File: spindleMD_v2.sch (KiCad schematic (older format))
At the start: 0 parts

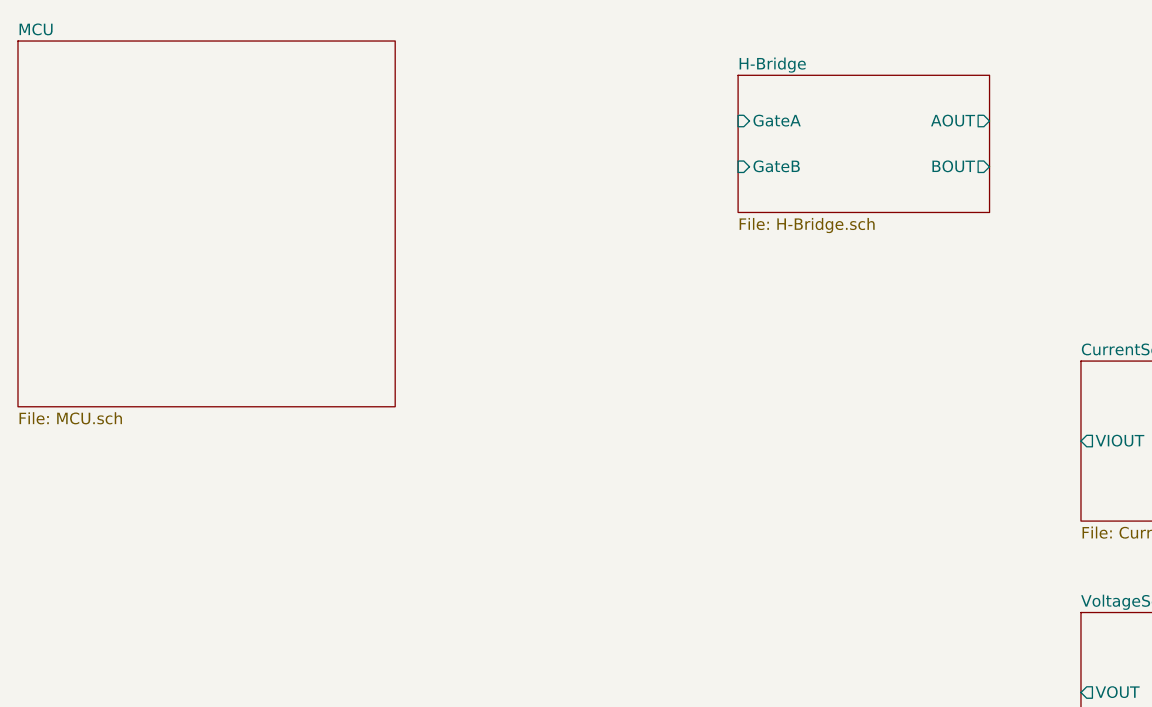
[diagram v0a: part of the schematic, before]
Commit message: デッドタイム挿入回路を削除、マイコンブロック作成
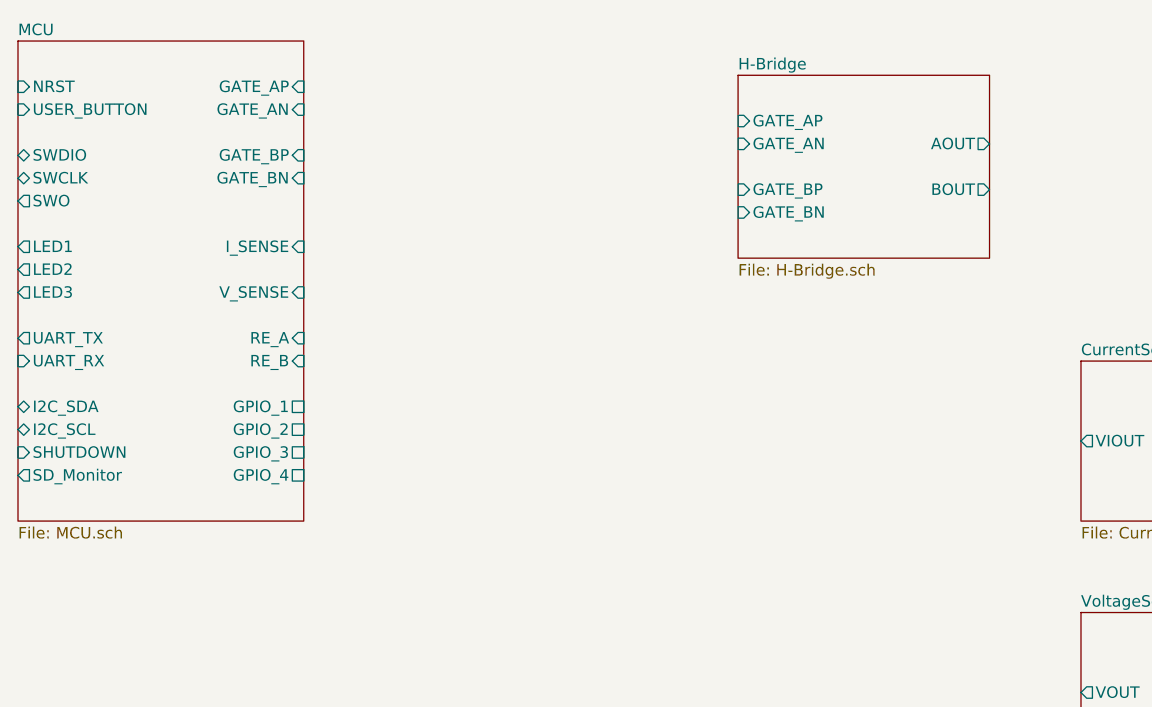
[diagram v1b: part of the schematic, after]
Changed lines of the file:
@@
 $EndDescr
 $Sheet
-S 3700 2550 1650 1600
+S 3700 2550 1250 2100
 U 5C77D603
 F0 "MCU" 50
 F1 "MCU.sch" 50
+F2 "NRST" I L 3700 2750 50
+F3 "SWDIO" B L 3700 3050 50
+F4 "SWCLK" B L 3700 3150 50
+F5 "SWO" O L 3700 3250 50
+F6 "I_SENSE" I R 4950 3450 50
+F7 "V_SENSE" I R 4950 3650 50
+F8 "GATE_AP" I R 4950 2750 50
+F9 "GATE_AN" I R 4950 2850 50
+F10 "GATE_BP" I R 4950 3050 50
+F11 "GATE_BN" I R 4950 3150 50
+F12 "UART_TX" O L 3700 3850 50
+F13 "UART_RX" I L 3700 3950 50
+F14 "I2C_SDA" B L 3700 4150 50
+F15 "I2C_SCL" B L 3700 4250 50
+F16 "RE_A" I R 4950 3850 50
+F17 "RE_B" I R 4950 3950 50
+F18 "LED1" O L 3700 3450 50
+F19 "LED2" O L 3700 3550 50
+F20 "LED3" O L 3700 3650 50
+F21 "USER_BUTTON" I L 3700 2850 50
+F22 "SD_Monitor" O L 3700 4450 50
+F23 "SHUTDOWN" I L 3700 4350 50
+F24 "GPIO_1" U R 4950 4150 50
+F25 "GPIO_2" U R 4950 4250 50
+F26 "GPIO_3" U R 4950 4350 50
+F27 "GPIO_4" U R 4950 4450 50
 $EndSheet
 $Sheet
-S 6850 2700 1100 600
+S 6850 2700 1100 800
 U 5C77D64E
 F0 "H-Bridge" 50
 F1 "H-Bridge.sch" 50
-F2 "AOUT" O R 7950 2900 50
-F3 "BOUT" O R 7950 3100 50
-F4 "GateA" I L 6850 2900 50
-F5 "GateB" I L 6850 3100 50
+F2 "AOUT" O R 7950 3000 50
+F3 "BOUT" O R 7950 3200 50
+F4 "GATE_AP" I L 6850 2900 50
+F5 "GATE_AN" I L 6850 3000 50
+F6 "GATE_BP" I L 6850 3200 50
+F7 "GATE_BN" I L 6850 3300 50
 $EndSheet
 $Sheet

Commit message: 第１版回路図完成
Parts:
- added C1, C2, C3, C4, C5, C6, C7, C8, C9: 0.1u, symbol Device:C_Small
- added C10: 100u, symbol Device:CP_Small
- added C11: 10u, symbol Device:CP_Small
- added D1, D5: D_Small, symbol Device:D_Small
- added D2: LED3, symbol Device:LED_Small
- added D3: LED2, symbol Device:LED_Small
- added D4: LED1, symbol Device:LED_Small
- added J1: Conn_LogicPower, symbol Connector_Generic:Conn_01x02
- added J2: Conn_SWD, symbol Connector_Generic:Conn_01x06
- added J3: Conn_UART, symbol Connector_Generic:Conn_01x04
- added J4: Conn_I2C, symbol Connector_Generic:Conn_01x06
- added J5: Conn_Encoder, symbol Connector_Generic:Conn_01x04
- added J6: Conn_GPIO, symbol Connector_Generic:Conn_01x06
- added J7: Conn_MotorPower, symbol Connector_Generic:Conn_01x02
- added J8: Conn_drivePower, symbol Connector_Generic:Conn_01x02
- added J9: Conn_Motor, symbol Connector_Generic:Conn_01x02
- added R1: 100, symbol Device:R_Small
- added R10, R2, R9: 10k, symbol Device:R_Small
- added R3: 470, symbol Device:R_Small
- added R4, R5, R6: 1k, symbol Device:R_Small
- added R7, R8: 2k, symbol Device:R_Small
- added SW1: USER_BUTTON, symbol Switch:SW_Push
- added SW2: RESET_BUTTON, symbol Switch:SW_Push
- added U1: L7805, symbol Regulator_Linear:L7805
- added U2: L78L33_SOT89, Package_TO_SOT_SMD:SOT-89-3, symbol Regulator_Linear:L78L33_SOT89
- added U3: IK0505SA, symbol mylib:IK0505SA
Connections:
- net CurrentSensing/IP+: now also J9.1 (Pin_1)
- net H-Bridge/AOUT: now also J9.2 (Pin_2)
- net MCU/GPIO_1: now also J6.3 (Pin_3)
- net MCU/GPIO_2: now also J6.4 (Pin_4)
- net MCU/GPIO_3: now also J6.5 (Pin_5)
- net MCU/GPIO_4: now also J6.6 (Pin_6)
- net MCU/I2C_SCL: now also J4.4 (Pin_4), R7.2
- net MCU/I2C_SDA: now also J4.3 (Pin_3), R8.2
- net MCU/LED1: now also D4.2 (A)
- net MCU/LED2: now also D3.2 (A)
- net MCU/LED3: now also D2.2 (A)
- net MCU/NRST: now also C2.1, J2.5 (Pin_5), SW2.2
- net MCU/RE_A: now also J5.3 (Pin_3), R10.1
- net MCU/RE_B: now also J5.4 (Pin_4), R9.1
- net MCU/SD_Monitor: now also J4.6 (Pin_6)
- net MCU/SHUTDOWN: now also J4.5 (Pin_5)
- net MCU/SWCLK: now also J2.2 (Pin_2)
- net MCU/SWDIO: now also J2.4 (Pin_4)
- net MCU/SWO: now also J2.6 (Pin_6)
- net MCU/UART_RX: now also J3.4 (Pin_4)
- net MCU/UART_TX: now also J3.3 (Pin_3)
- net MCU/USER_BUTTON: now also R3.1
- new net: C1.2, R2.1, R3.2, SW1.2
- new net: D4.1 (K), R6.1
- new net: D3.1 (K), R5.1
- new net: D2.1 (K), R4.1
- new net: C3.1, D1.1 (K), J1.2 (Pin_2), U1.1 (IN)
- new net: C1.1, R1.2
- new net +12V: C11.1, J8.2 (Pin_2)
- new net +3V3: C6.1, D5.2 (A), J2.1 (Pin_1), J3.2 (Pin_2), J6.2 (Pin_2), R1.1, R10.2, R7.1, R8.1, R9.2, SW1.1, U2.1 (OUT)
- new net +5V: C4.1, C5.1, C7.1, C8.1, D1.2 (A), D5.1 (K), J5.2 (Pin_2), U1.3 (OUT), U2.3 (IN), U3.2 (+VIN)
- new net +5VA: C9.1, U3.4 (+VOUT)
- new net GND: C2.2, C3.2, C4.2, C5.2, C6.2, C7.2, C8.2, J1.1 (Pin_1), J2.3 (Pin_3), J3.1 (Pin_1), J4.1 (Pin_1), J5.1 (Pin_1), J6.1 (Pin_1), R2.2, R4.2, R5.2, R6.2, SW2.1, U1.2 (GND), U2.2 (GND), U3.1 (-VIN)
- new net GNDPWR: C10.2, C11.2, C9.2, J7.1 (Pin_1), J8.1 (Pin_1), U3.3 (-VOUT)
- new net VDD: C10.1, J7.2 (Pin_2)
- no-connect marks 0 -> 1

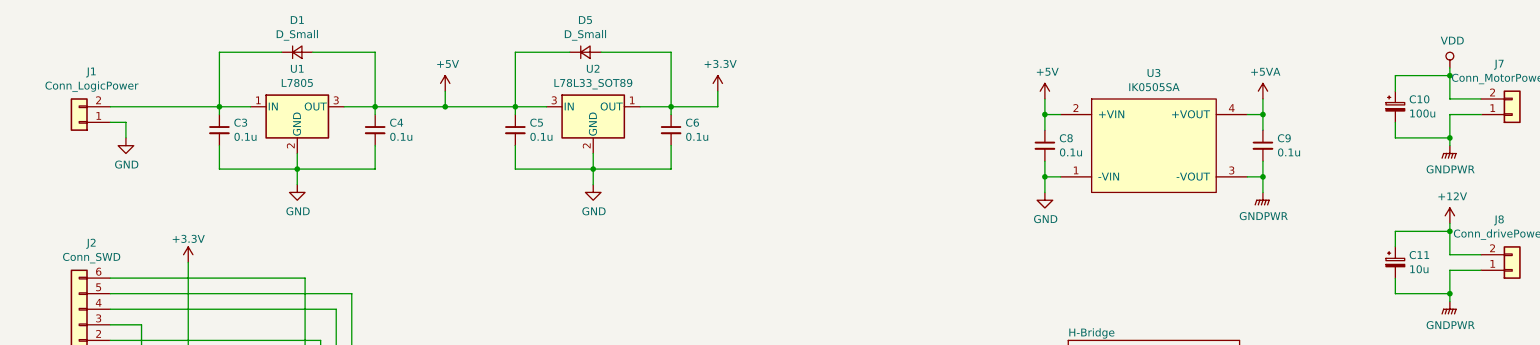
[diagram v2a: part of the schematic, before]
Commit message: powerFlag追加
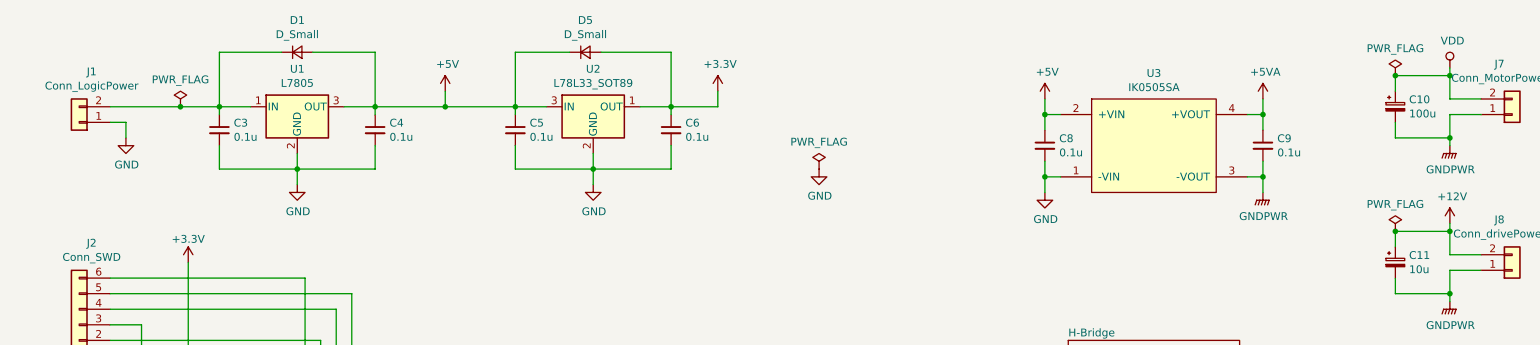
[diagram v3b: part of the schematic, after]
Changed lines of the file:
@@
 Wire Wire Line
 	10350 1350 10550 1350
-Wire Wire Line
-	1750 1400 2450 1400
 $Comp
 L Connector_Generic:Conn_01x02 J9
@@
 Wire Wire Line
 	850  3850 850  3950
+$Comp
+L power:GND #PWR?
+U 1 1 5C7D9F11
+P 6300 1800
+AR Path="/5C77D64E/5C7D9F11" Ref="#PWR?"  Part="1"
+AR Path="/5C7D9F11" Ref="#PWR0101"  Part="1"
+F 0 "#PWR0101" H 6300 1550 50  0001 C CNN
+F 1 "GND" H 6305 1627 50  0000 C CNN
+F 2 "" H 6300 1800 50  0001 C CNN
+F 3 "" H 6300 1800 50  0001 C CNN
+	1    6300 1800
+	1    0    0    -1
+$EndComp
+$Comp
+L power:PWR_FLAG #FLG0101
+U 1 1 5C7E63D3
+P 2200 1400
+F 0 "#FLG0101" H 2200 1475 50  0001 C CNN
+F 1 "PWR_FLAG" H 2200 1574 50  0000 C CNN
+F 2 "" H 2200 1400 50  0001 C CNN
+F 3 "~" H 2200 1400 50  0001 C CNN
+	1    2200 1400
+	1    0    0    -1
+$EndComp
+Wire Wire Line
+	2200 1400 2450 1400
+Connection ~ 2200 1400
+Wire Wire Line
+	1750 1400 2200 1400
+$Comp
+L power:PWR_FLAG #FLG0102
+U 1 1 5C7F1DF2
+P 6300 1800
+F 0 "#FLG0102" H 6300 1875 50  0001 C CNN
+F 1 "PWR_FLAG" H 6300 1974 50  0000 C CNN
+F 2 "" H 6300 1800 50  0001 C CNN
+F 3 "~" H 6300 1800 50  0001 C CNN
+	1    6300 1800
+	1    0    0    -1
+$EndComp
+$Comp
+L power:PWR_FLAG #FLG0103
+U 1 1 5C7F217D
+P 10000 2200
+F 0 "#FLG0103" H 10000 2275 50  0001 C CNN
+F 1 "PWR_FLAG" H 10000 2374 50  0000 C CNN
+F 2 "" H 10000 2200 50  0001 C CNN
+F 3 "~" H 10000 2200 50  0001 C CNN
+	1    10000 2200
+	1    0    0    -1
+$EndComp
+Connection ~ 10000 2200
+$Comp
+L power:PWR_FLAG #FLG0104
+U 1 1 5C815D89
+P 10000 1200
+F 0 "#FLG0104" H 10000 1275 50  0001 C CNN
+F 1 "PWR_FLAG" H 10000 1374 50  0000 C CNN
+F 2 "" H 10000 1200 50  0001 C CNN
+F 3 "~" H 10000 1200 50  0001 C CNN
+	1    10000 1200
+	1    0    0    -1
+$EndComp
+Connection ~ 10000 1200
 $EndSCHEMATC

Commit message: フットプリント割り付け＆Netリスト出力
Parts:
- C1, C2, C3, C4, C5, C6, C7, C8, C9: footprint (none) -> Capacitors_SMD:C_0805_HandSoldering
- C10: footprint (none) -> Capacitors_THT:CP_Radial_D10.0mm_P5.00mm
- C11: footprint (none) -> Capacitors_SMD:C_0603_HandSoldering
- D1, D5: footprint (none) -> Diodes_SMD:D_TUMD2
- D2, D3, D4: footprint (none) -> LEDs:LED_0603_HandSoldering
- J1, J8: footprint (none) -> Connectors_JST:JST_XH_B02B-XH-A_02x2.50mm_Straight
- J2, J4, J6: footprint (none) -> Connectors_JST:JST_XH_B06B-XH-A_06x2.50mm_Straight
- J3, J5: footprint (none) -> Connectors_JST:JST_XH_B04B-XH-A_04x2.50mm_Straight
- J7, J9: footprint (none) -> Connectors_JST:JST_VH_B2P-VH-B_2x3.96mm_Vertical
- R1, R10, R2, R3, R4, R5, R6, R7, R8, R9: footprint (none) -> Resistors_SMD:R_0603_HandSoldering
- SW1, SW2: footprint (none) -> my_footPrint:LS6J2M
- U1: footprint (none) -> TO_SOT_Packages_SMD:TO-252-2_Rectifier
- U2: footprint Package_TO_SOT_SMD:SOT-89-3 -> TO_SOT_Packages_SMD:SOT-89-3_Handsoldering
- U3: footprint (none) -> my_footPrint:IK0505SA
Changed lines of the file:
@@
 F 0 "U3" H 8450 2115 50  0000 C CNN
 F 1 "IK0505SA" H 8450 2024 50  0000 C CNN
-F 2 "" H 8450 1650 50  0001 C CNN
+F 2 "my_footPrint:IK0505SA" H 8450 1650 50  0001 C CNN
 F 3 "" H 8450 1650 50  0001 C CNN
 	1    8450 1650
@@
 F 0 "C9" H 9242 1696 50  0000 L CNN
 F 1 "0.1u" H 9242 1605 50  0000 L CNN
-F 2 "" H 9150 1650 50  0001 C CNN
+F 2 "Capacitors_SMD:C_0805_HandSoldering" H 9150 1650 50  0001 C CNN
 F 3 "~" H 9150 1650 50  0001 C CNN
 	1    9150 1650
@@
 F 0 "C8" H 7842 1696 50  0000 L CNN
 F 1 "0.1u" H 7842 1605 50  0000 L CNN
-F 2 "" H 7750 1650 50  0001 C CNN
+F 2 "Capacitors_SMD:C_0805_HandSoldering" H 7750 1650 50  0001 C CNN
 F 3 "~" H 7750 1650 50  0001 C CNN
 	1    7750 1650
@@
 F 0 "SW2" H 2300 4035 50  0000 C CNN
 F 1 "RESET_BUTTON" H 2300 3944 50  0000 C CNN
-F 2 "" H 2300 3950 50  0001 C CNN
+F 2 "my_footPrint:LS6J2M" H 2300 3950 50  0001 C CNN
 F 3 "" H 2300 3950 50  0001 C CNN
 	1    2300 3750
@@
 F 0 "J4" H 1470 6175 50  0000 C CNN
 F 1 "Conn_I2C" H 1470 6266 50  0000 C CNN
-F 2 "" H 1550 6700 50  0001 C CNN
+F 2 "Connectors_JST:JST_XH_B06B-XH-A_06x2.50mm_Straight" H 1550 6700 50  0001 C CNN
 F 3 "~" H 1550 6700 50  0001 C CNN
 	1    1550 6700
@@
 F 0 "J3" H 1470 5175 50  0000 C CNN
 F 1 "Conn_UART" H 1470 5266 50  0000 C CNN
-F 2 "" H 1550 5600 50  0001 C CNN
+F 2 "Connectors_JST:JST_XH_B04B-XH-A_04x2.50mm_Straight" H 1550 5600 50  0001 C CNN
 F 3 "~" H 1550 5600 50  0001 C CNN
 	1    1550 5600
@@
 F 0 "SW1" V 1100 4200 50  0000 L CNN
 F 1 "USER_BUTTON" V 1000 4200 50  0000 L CNN
-F 2 "" H 1050 4250 50  0001 C CNN
+F 2 "my_footPrint:LS6J2M" H 1050 4250 50  0001 C CNN
 F 3 "" H 1050 4250 50  0001 C CNN
 	1    1050 4050
@@
 F 0 "D4" H 3400 4785 50  0000 C CNN
 F 1 "LED1" H 3400 4694 50  0000 C CNN
-F 2 "" V 3400 4550 50  0001 C CNN
+F 2 "LEDs:LED_0603_HandSoldering" V 3400 4550 50  0001 C CNN
 F 3 "~" V 3400 4550 50  0001 C CNN
 	1    3400 4550
@@
 F 0 "D3" H 3200 4885 50  0000 C CNN
 F 1 "LED2" H 3200 4794 50  0000 C CNN
-F 2 "" V 3200 4650 50  0001 C CNN
+F 2 "LEDs:LED_0603_HandSoldering" V 3200 4650 50  0001 C CNN
 F 3 "~" V 3200 4650 50  0001 C CNN
 	1    3200 4650
@@
 F 0 "D2" H 3000 4985 50  0000 C CNN
 F 1 "LED3" H 3000 4894 50  0000 C CNN
-F 2 "" V 3000 4750 50  0001 C CNN
+F 2 "LEDs:LED_0603_HandSoldering" V 3000 4750 50  0001 C CNN
 F 3 "~" V 3000 4750 50  0001 C CNN
 	1    3000 4750
@@
 F 0 "R6" V 2604 4550 50  0000 C CNN
 F 1 "1k" V 2695 4550 50  0000 C CNN
-F 2 "" H 2800 4550 50  0001 C CNN
+F 2 "Resistors_SMD:R_0603_HandSoldering" H 2800 4550 50  0001 C CNN
 F 3 "~" H 2800 4550 50  0001 C CNN
 	1    2800 4550
@@
 F 0 "R5" V 2404 4650 50  0000 C CNN
 F 1 "1k" V 2495 4650 50  0000 C CNN
-F 2 "" H 2600 4650 50  0001 C CNN
+F 2 "Resistors_SMD:R_0603_HandSoldering" H 2600 4650 50  0001 C CNN
 F 3 "~" H 2600 4650 50  0001 C CNN
 	1    2600 4650
@@
 F 0 "R4" V 2204 4750 50  0000 C CNN
 F 1 "1k" V 2295 4750 50  0000 C CNN
-F 2 "" H 2400 4750 50  0001 C CNN
+F 2 "Resistors_SMD:R_0603_HandSoldering" H 2400 4750 50  0001 C CNN
 F 3 "~" H 2400 4750 50  0001 C CNN
 	1    2400 4750
@@
 F 0 "R3" V 1554 4350 50  0000 C CNN
 F 1 "470" V 1645 4350 50  0000 C CNN
-F 2 "" H 1750 4350 50  0001 C CNN
+F 2 "Resistors_SMD:R_0603_HandSoldering" H 1750 4350 50  0001 C CNN
 F 3 "~" H 1750 4350 50  0001 C CNN
 	1    1750 4350
@@
 F 0 "R2" H 1109 4646 50  0000 L CNN
 F 1 "10k" H 1109 4555 50  0000 L CNN
-F 2 "" H 1050 4600 50  0001 C CNN
+F 2 "Resistors_SMD:R_0603_HandSoldering" H 1050 4600 50  0001 C CNN
 F 3 "~" H 1050 4600 50  0001 C CNN
 	1    1050 4600
@@
 F 0 "J2" H 1470 2275 50  0000 C CNN
 F 1 "Conn_SWD" H 1470 2366 50  0000 C CNN
-F 2 "" H 1550 2800 50  0001 C CNN
+F 2 "Connectors_JST:JST_XH_B06B-XH-A_06x2.50mm_Straight" H 1550 2800 50  0001 C CNN
 F 3 "~" H 1550 2800 50  0001 C CNN
 	1    1550 2800
@@
 F 0 "J5" H 6569 5225 50  0000 C CNN
 F 1 "Conn_Encoder" H 6569 5316 50  0000 C CNN
-F 2 "" H 6650 5650 50  0001 C CNN
+F 2 "Connectors_JST:JST_XH_B04B-XH-A_04x2.50mm_Straight" H 6650 5650 50  0001 C CNN
 F 3 "~" H 6650 5650 50  0001 C CNN
 	1    6650 5650
@@
 F 0 "R10" V 5954 5550 50  0000 C CNN
 F 1 "10k" V 6045 5550 50  0000 C CNN
-F 2 "" H 6150 5550 50  0001 C CNN
+F 2 "Resistors_SMD:R_0603_HandSoldering" H 6150 5550 50  0001 C CNN
 F 3 "~" H 6150 5550 50  0001 C CNN
 	1    6150 5550
@@
 F 0 "R9" V 5754 5450 50  0000 C CNN
 F 1 "10k" V 5845 5450 50  0000 C CNN
-F 2 "" H 5950 5450 50  0001 C CNN
+F 2 "Resistors_SMD:R_0603_HandSoldering" H 5950 5450 50  0001 C CNN
 F 3 "~" H 5950 5450 50  0001 C CNN
 	1    5950 5450
@@
 F 0 "J6" H 6569 6175 50  0000 C CNN
 F 1 "Conn_GPIO" H 6569 6266 50  0000 C CNN
-F 2 "" H 6650 6700 50  0001 C CNN
+F 2 "Connectors_JST:JST_XH_B06B-XH-A_06x2.50mm_Straight" H 6650 6700 50  0001 C CNN
 F 3 "~" H 6650 6700 50  0001 C CNN
 	1    6650 6700
@@
 F 0 "J1" H 1470 1175 50  0000 C CNN
 F 1 "Conn_LogicPower" H 1470 1266 50  0000 C CNN
-F 2 "" H 1550 1500 50  0001 C CNN
+F 2 "Connectors_JST:JST_XH_B02B-XH-A_02x2.50mm_Straight" H 1550 1500 50  0001 C CNN
 F 3 "~" H 1550 1500 50  0001 C CNN
 	1    1550 1500
@@
 F 0 "U1" H 2950 1642 50  0000 C CNN
 F 1 "L7805" H 2950 1551 50  0000 C CNN
-F 2 "" H 2975 1250 50  0001 L CIN
+F 2 "TO_SOT_Packages_SMD:TO-252-2_Rectifier" H 2975 1250 50  0001 L CIN
 F 3 "http://www.st.com/content/ccc/resource/technical/document/datasheet/41/4f/b3/b0/12/d4/47/88/CD00000444.pdf/files/CD00000444.pdf/jcr:content/translations/en.CD00000444.pdf" H 2950 1350 50  0001 C CNN
 	1    2950 1400
@@
 F 0 "C3" H 2542 1596 50  0000 L CNN
 F 1 "0.1u" H 2542 1505 50  0000 L CNN
-F 2 "" H 2450 1550 50  0001 C CNN
+F 2 "Capacitors_SMD:C_0805_HandSoldering" H 2450 1550 50  0001 C CNN
 F 3 "~" H 2450 1550 50  0001 C CNN
 	1    2450 1550
@@
 F 0 "C4" H 3542 1596 50  0000 L CNN
 F 1 "0.1u" H 3542 1505 50  0000 L CNN
-F 2 "" H 3450 1550 50  0001 C CNN
+F 2 "Capacitors_SMD:C_0805_HandSoldering" H 3450 1550 50  0001 C CNN
 F 3 "~" H 3450 1550 50  0001 C CNN
 	1    3450 1550
@@
 F 0 "D1" H 2950 1255 50  0000 C CNN
 F 1 "D_Small" H 2950 1164 50  0000 C CNN
-F 2 "" V 2950 1050 50  0001 C CNN
+F 2 "Diodes_SMD:D_TUMD2" V 2950 1050 50  0001 C CNN
 F 3 "~" V 2950 1050 50  0001 C CNN
 	1    2950 1050
@@
 F 0 "U2" H 4850 1642 50  0000 C CNN
 F 1 "L78L33_SOT89" H 4850 1551 50  0000 C CNN
-F 2 "Package_TO_SOT_SMD:SOT-89-3" H 4850 1600 50  0001 C CIN
+F 2 "TO_SOT_Packages_SMD:SOT-89-3_Handsoldering" H 4850 1600 50  0001 C CIN
 F 3 "http://www.st.com/content/ccc/resource/technical/document/datasheet/15/55/e5/aa/23/5b/43/fd/CD00000446.pdf/files/CD00000446.pdf/jcr:content/translations/en.CD00000446.pdf" H 4850 1350 50  0001 C CNN
 	1    4850 1400
@@
 F 0 "C5" H 4442 1596 50  0000 L CNN
 F 1 "0.1u" H 4442 1505 50  0000 L CNN
-F 2 "" H 4350 1550 50  0001 C CNN
+F 2 "Capacitors_SMD:C_0805_HandSoldering" H 4350 1550 50  0001 C CNN
 F 3 "~" H 4350 1550 50  0001 C CNN
 	1    4350 1550
@@
 F 0 "D5" H 4800 1255 50  0000 C CNN
 F 1 "D_Small" H 4800 1164 50  0000 C CNN
-F 2 "" V 4800 1050 50  0001 C CNN
+F 2 "Diodes_SMD:D_TUMD2" V 4800 1050 50  0001 C CNN
 F 3 "~" V 4800 1050 50  0001 C CNN
 	1    4800 1050
@@
 F 0 "C6" H 5442 1596 50  0000 L CNN
 F 1 "0.1u" H 5442 1505 50  0000 L CNN
-F 2 "" H 5350 1550 50  0001 C CNN
+F 2 "Capacitors_SMD:C_0805_HandSoldering" H 5350 1550 50  0001 C CNN
 F 3 "~" H 5350 1550 50  0001 C CNN
 	1    5350 1550
@@
 F 0 "J8" H 10669 2125 50  0000 C CNN
 F 1 "Conn_drivePower" H 10669 2216 50  0000 C CNN
-F 2 "" H 10750 2450 50  0001 C CNN
+F 2 "Connectors_JST:JST_XH_B02B-XH-A_02x2.50mm_Straight" H 10750 2450 50  0001 C CNN
 F 3 "~" H 10750 2450 50  0001 C CNN
 	1    10750 2450
@@
 F 0 "J7" H 10669 1125 50  0000 C CNN
 F 1 "Conn_MotorPower" H 10669 1216 50  0000 C CNN
-F 2 "" H 10750 1450 50  0001 C CNN
+F 2 "Connectors_JST:JST_VH_B2P-VH-B_2x3.96mm_Vertical" H 10750 1450 50  0001 C CNN
 F 3 "~" H 10750 1450 50  0001 C CNN
 	1    10750 1450
@@
 F 0 "J9" H 10669 2975 50  0000 C CNN
 F 1 "Conn_Motor" H 10669 3066 50  0000 C CNN
-F 2 "" H 10750 3300 50  0001 C CNN
+F 2 "Connectors_JST:JST_VH_B2P-VH-B_2x3.96mm_Vertical" H 10750 3300 50  0001 C CNN
 F 3 "~" H 10750 3300 50  0001 C CNN
 	1    10750 3300
@@
 F 0 "C10" H 10088 1446 50  0000 L CNN
 F 1 "100u" H 10088 1355 50  0000 L CNN
-F 2 "" H 10000 1400 50  0001 C CNN
+F 2 "Capacitors_THT:CP_Radial_D10.0mm_P5.00mm" H 10000 1400 50  0001 C CNN
 F 3 "~" H 10000 1400 50  0001 C CNN
 	1    10000 1400
@@
 F 0 "C11" H 10088 2446 50  0000 L CNN
 F 1 "10u" H 10088 2355 50  0000 L CNN
-F 2 "" H 10000 2400 50  0001 C CNN
+F 2 "Capacitors_SMD:C_0603_HandSoldering" H 10000 2400 50  0001 C CNN
 F 3 "~" H 10000 2400 50  0001 C CNN
 	1    10000 2400
@@
 F 0 "R8" V 3204 6700 50  0000 C CNN
 F 1 "2k" V 3295 6700 50  0000 C CNN
-F 2 "" H 3400 6700 50  0001 C CNN
+F 2 "Resistors_SMD:R_0603_HandSoldering" H 3400 6700 50  0001 C CNN
 F 3 "~" H 3400 6700 50  0001 C CNN
 	1    3400 6700
@@
 F 0 "R7" V 3004 6600 50  0000 C CNN
 F 1 "2k" V 3095 6600 50  0000 C CNN
-F 2 "" H 3200 6600 50  0001 C CNN
+F 2 "Resistors_SMD:R_0603_HandSoldering" H 3200 6600 50  0001 C CNN
 F 3 "~" H 3200 6600 50  0001 C CNN
 	1    3200 6600
@@
 F 0 "C7" H 6042 5846 50  0000 L CNN
 F 1 "0.1u" H 6042 5755 50  0000 L CNN
-F 2 "" H 5950 5800 50  0001 C CNN
+F 2 "Capacitors_SMD:C_0805_HandSoldering" H 5950 5800 50  0001 C CNN
 F 3 "~" H 5950 5800 50  0001 C CNN
 	1    5950 5800
@@
 F 0 "C2" V 2500 3950 50  0000 C CNN
 F 1 "0.1u" V 2400 3950 50  0000 C CNN
-F 2 "" H 2300 3950 50  0001 C CNN
+F 2 "Capacitors_SMD:C_0805_HandSoldering" H 2300 3950 50  0001 C CNN
 F 3 "~" H 2300 3950 50  0001 C CNN
 	1    2300 3950
@@
 F 0 "C1" H 700 4100 50  0000 L CNN
 F 1 "0.1u" H 650 4000 50  0000 L CNN
-F 2 "" H 850 4050 50  0001 C CNN
+F 2 "Capacitors_SMD:C_0805_HandSoldering" H 850 4050 50  0001 C CNN
 F 3 "~" H 850 4050 50  0001 C CNN
 	1    850  4050
@@
 F 0 "R1" H 1000 3800 50  0000 R CNN
 F 1 "100" H 1050 3700 50  0000 R CNN
-F 2 "" H 850 3750 50  0001 C CNN
+F 2 "Resistors_SMD:R_0603_HandSoldering" H 850 3750 50  0001 C CNN
 F 3 "~" H 850 3750 50  0001 C CNN
 	1    850  3750
